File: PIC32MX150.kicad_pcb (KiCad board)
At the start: 2 copper layers, 28 parts, among them J1 GPIO_1, J2 USB_B_Micro, J3 Barrel_Jack, J4 ICSP, J5 GPIO_2, SW1 RST, SW2 SW_SPDT, U1 PIC32MX150F128D-IPT, U2 LM22676MR-ADJ, U3 CH340C

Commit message: LO
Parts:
- added C13: 10p, Capacitor_SMD:C_0603_1608Metric_Pad1.08x0.95mm_HandSolder, F.Cu at (96.3, 54.6)
- added C14: 10p, Capacitor_SMD:C_0603_1608Metric_Pad1.08x0.95mm_HandSolder, F.Cu at (103.5, 61.8)
- added C15: 1u, Capacitor_SMD:C_0603_1608Metric_Pad1.08x0.95mm_HandSolder, F.Cu at (75.8, 52.6)
- added C16: 100n, Capacitor_SMD:C_0603_1608Metric_Pad1.08x0.95mm_HandSolder, F.Cu at (78.6, 52.6)
- added C17: 100n, Capacitor_SMD:C_0603_1608Metric_Pad1.08x0.95mm_HandSolder, F.Cu at (60.6, 47.2)
- added C18: 100n, Capacitor_SMD:C_0603_1608Metric_Pad1.08x0.95mm_HandSolder, F.Cu at (62.1, 88.4)
- added D2: LED_B, LED_SMD:LED_0603_1608Metric_Pad1.05x0.95mm_HandSolder, F.Cu at (56.5, 63.4)
- added D3: LED_B, LED_SMD:LED_0603_1608Metric_Pad1.05x0.95mm_HandSolder, F.Cu at (58.8, 63.4)
- added D4: LED_G, LED_SMD:LED_0603_1608Metric_Pad1.05x0.95mm_HandSolder, F.Cu at (54.5, 53.3)
- added JP1: Jumper_NO_Small, Jumper:SolderJumper-2_P1.3mm_Open_Pad1.0x1.5mm, B.Cu at (108.9, 72.2)
- added R5: 1M, Resistor_SMD:R_0603_1608Metric_Pad0.98x0.95mm_HandSolder, F.Cu at (96.3, 60.8)
- added R6: 1.5K, Resistor_SMD:R_0603_1608Metric_Pad0.98x0.95mm_HandSolder, F.Cu at (60.6, 55.2)
- added R7: 1K, Resistor_SMD:R_0603_1608Metric_Pad0.98x0.95mm_HandSolder, B.Cu at (51.4, 49.3)
- added Y1: TSX3225, Crystal:Crystal_SMD_SeikoEpson_TSX3225-4Pin_3.2x2.5mm_HandSoldering, F.Cu at (100.0, 58.3)
- C12, U3: moved to F.Cu
- C7, R1: moved to B.Cu
- J1: footprint Connector_PinHeader_2.54mm:PinHeader_2x12_P2.54mm_Vertical -> Connector_PinSocket_2.54mm:PinSocket_2x12_P2.54mm_Vertical
- L1: footprint Inductor_SMD:L_0805_2012Metric_Pad1.15x1.40mm_HandSolder -> Inductor_SMD:L_Taiyo-Yuden_MD-1616
- SW2: footprint Button_Switch_THT:SW_Slide_1P2T_CK_OS102011MS2Q -> Custom_Libs:SPDT_SW_Big
- moved D1 51.2 mm to (76.8, 46.2), turned to 0 degrees
- moved L1 50.1 mm to (66.2, 45.2)
- moved R4 48.3 mm to (60.6, 51.1), turned to 270 degrees
- moved C11 48.1 mm to (55.0, 47.1), turned to 90 degrees
- moved C8 42.4 mm to (43.1, 49.4), turned to 90 degrees
- moved C10 41.9 mm to (69.7, 48.3)
- moved C9 38.3 mm to (47.9, 47.1), turned to 90 degrees
- moved R3 37.1 mm to (63.0, 51.1), turned to 90 degrees
- moved U2 35.5 mm to (69.7, 52.3), turned to 0 degrees
- moved U3 20.1 mm to (58.5, 81.3), turned to 270 degrees
- moved J1 14.8 mm to (72.1, 88.9)
- moved J2 12.4 mm to (42.7, 81.5)
- moved SW1 11.9 mm to (106.7, 87.4)
- moved J3 11.8 mm to (50.4, 67.1)
- moved C2 9.85 mm to (98.5, 77.0), turned to 315 degrees
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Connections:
- R1 pad 2: Net-(C7-Pad1) -> Net-(JP1-Pad1)
- R2 pad 2: Net-(C7-Pad1) -> Net-(JP1-Pad1)
- U1 pad 30: (no net) -> /OSC1
- U1 pad 31: (no net) -> /OSC2
- U2 pad 5: (no net) -> GND
- U3 pad 16: +5V -> +3V3
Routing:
- net +3V3: track 0.00 -> 76.6 mm, vias 0 -> 5
- net +5V: track 0.00 -> 49.7 mm
- net /PWR_USB: track 0.00 -> 37.7 mm
- net Net-(J2-Pad2): track 0.00 -> 17.4 mm
- net Net-(J2-Pad3): track 0.00 -> 15.8 mm
- net /OSC1: track 0.00 -> 14.7 mm
- net /PWR_DC: track 0.00 -> 14.0 mm, vias 0 -> 1
- net /OSC2: track 0.00 -> 12.3 mm
- net Net-(D2-Pad1): track 0.00 -> 8.91 mm
- net Net-(R3-Pad1): track 0.00 -> 7.32 mm
- net /MCLR: track 0.00 -> 5.28 mm
- net Net-(D4-Pad1): track 0.00 -> 4.58 mm, vias 0 -> 1
- net Net-(C10-Pad2): track 0.00 -> 3.79 mm
- net Net-(C12-Pad1): track 0.00 -> 2.76 mm
- net GND: vias 0 -> 6
- added copper zone on F.Cu, net +3V3
- added copper zone on F.Cu, net +5V
- added copper zone on F.Cu, net /PWR_DC
- added copper zone on F.Cu, net GND
- added copper zone on F.Cu, net Net-(C10-Pad1)
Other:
- board outline added: 80 x 55 mm
- net class Default: clearance 0.254 -> 0.2032; via_dia 0.508 -> 0.635; via_drill 0.3048 -> 0.381
- net class PWR added: clearance 0.2032, trace_width 0.508, via_dia 0.762, via_drill 0.508
- rule trace_clearance: 0.254 -> 0.2032

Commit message: inductor
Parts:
- removed D2, D3: LED_B, LED_SMD:LED_0603_1608Metric_Pad1.05x0.95mm_HandSolder
- removed R6: 1.5K, Resistor_SMD:R_0603_1608Metric_Pad0.98x0.95mm_HandSolder
- L1: value 8.2u -> 22u; footprint Inductor_SMD:L_Taiyo-Yuden_MD-1616 -> Inductor_SMD:L_Taiyo-Yuden_NR-80xx_HandSoldering
- moved C18 13.0 mm to (61.6, 75.4), turned to 90 degrees
- moved C12 10.1 mm to (49.6, 78.4), turned to 180 degrees
- moved R3 6.59 mm to (59.9, 56.9)
- moved U2 6.56 mm to (66.3, 57.9)
- moved J5 6.48 mm to (111.5, 45.0)
- moved R4 6.32 mm to (58.2, 56.9)
- moved C17 6.28 mm to (59.1, 53.3), turned to 0 degrees
- moved C10 6.13 mm to (66.3, 53.3)
- moved C16 5.58 mm to (73.4, 54.5), turned to 0 degrees
- moved C15 5.32 mm to (73.4, 57.3), turned to 0 degrees
- moved C8 5.12 mm to (46.4, 53.3), turned to 180 degrees
- moved R7 4.13 mm to (48.8, 52.4)
- moved D1 3.91 mm to (75.9, 50.0)
- moved U3 3.71 mm to (55.6, 79.0), turned to 0 degrees
- moved L1 2.45 mm to (65.3, 47.5)
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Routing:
- net +3V3: track 76.6 -> 99.0 mm, vias 5 -> 4
- net /PWR_DC: track 14.0 -> 0.00 mm, vias 1 -> 0
- net /PWR_USB: track 37.7 -> 27.2 mm, vias 0 -> 1
- net Net-(D2-Pad1): track 8.91 -> 0.00 mm
- net Net-(J2-Pad2): track 17.4 -> 9.03 mm
- net Net-(J2-Pad3): track 15.8 -> 18.2 mm
- net /MCLR: track 5.28 -> 3.89 mm
- net /OSC2: track 12.3 -> 11.0 mm
- net GND: track 0.00 -> 1.22 mm, vias 6 -> 42
- net Net-(R3-Pad1): track 7.32 -> 6.18 mm
- net Net-(D4-Pad1): track 4.58 -> 3.44 mm
- net /OSC1: track 14.7 -> 13.7 mm
- net +5V: track 49.7 -> 50.6 mm
- added copper zone on B.Cu, net GND
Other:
- net class Default: via_dia 0.635 -> 0.508; via_drill 0.381 -> 0.3048

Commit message: gerber
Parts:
- added D2: LED_R, LED_SMD:LED_0603_1608Metric_Pad1.05x0.95mm_HandSolder, F.Cu at (108.5, 52.6)
- added D3: LED_B, LED_SMD:LED_0603_1608Metric_Pad1.05x0.95mm_HandSolder, F.Cu at (105.4, 52.6)
- added D5: LED_R, LED_SMD:LED_0603_1608Metric_Pad1.05x0.95mm_HandSolder, F.Cu at (65.7, 80.5)
- added D6: LED_B, LED_SMD:LED_0603_1608Metric_Pad1.05x0.95mm_HandSolder, F.Cu at (63.4, 80.5)
- added G***: LOGO, Custom_Libs:microchip_logo, F.Cu at (63.2, 65.5)
- added G***: LOGO, Custom_Libs:PIC32_Logo, F.Cu at (64.3, 68.3)
- added G***: LOGO, Custom_Libs:OS_Hardware, F.Cu at (106.2, 83.1)
- added J6: SPI_0, Connector_Molex:Molex_PicoBlade_53261-0471_1x04-1MP_P1.25mm_Horizontal, F.Cu at (63.2, 90.7)
- added J7: SPI_1, Connector_Molex:Molex_PicoBlade_53261-0471_1x04-1MP_P1.25mm_Horizontal, F.Cu at (49.0, 90.7)
- added R10: 1K, Resistor_SMD:R_0603_1608Metric_Pad0.98x0.95mm_HandSolder, F.Cu at (61.1, 80.5)
- added R11: 50K, Resistor_SMD:R_0603_1608Metric_Pad0.98x0.95mm_HandSolder, F.Cu at (116.3, 63.0)
- added R6: 1K, Resistor_SMD:R_0603_1608Metric_Pad0.98x0.95mm_HandSolder, B.Cu at (108.6, 56.9)
- added R8: 1K, Resistor_SMD:R_0603_1608Metric_Pad0.98x0.95mm_HandSolder, B.Cu at (108.6, 58.9)
- added R9: 1K, Resistor_SMD:R_0603_1608Metric_Pad0.98x0.95mm_HandSolder, F.Cu at (67.9, 80.5)
- added SW3: SW_SPST, Button_Switch_SMD:SW_SPST_PTS645, F.Cu at (114.8, 52.6)
- L1: footprint Inductor_SMD:L_Taiyo-Yuden_NR-80xx_HandSoldering -> Inductor_SMD:L_Sumida_CDMC6D28_7.25x6.5mm
- SW1: footprint Button_Switch_THT:SW_TH_Tactile_Omron_B3F-10xx -> Button_Switch_SMD:SW_SPST_B3U-1000P
- moved SW1 15.5 mm to (109.7, 72.1)
- moved JP1 5.45 mm to (104.6, 75.7), turned to 90 degrees
- moved C1 4.72 mm to (99.1, 63.8)
- moved R1 4.57 mm to (101.1, 76.7), turned to 0 degrees
- moved C7 4.53 mm to (101.1, 74.7), turned to 180 degrees
- moved C5 3.97 mm to (97.5, 62.2)
- moved U1 3.45 mm to (87.9, 67.2)
- moved R2 3.45 mm to (96.4, 72.8)
- moved R5 3.45 mm to (93.5, 58.8)
- moved C13 3.45 mm to (93.8, 53.2)
- moved C2 3.45 mm to (95.0, 74.3)
- moved C3 3.45 mm to (79.1, 58.3)
- moved C14 3.45 mm to (100.6, 59.2)
- moved C4 3.45 mm to (81.1, 60.3)
- moved Y1 3.45 mm to (97.2, 56.2)
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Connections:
- net /RB2 renamed /RB2|SDA2
- net /RB3 renamed /RB3|SCL2
- J1 pad 10: GND -> /RC8|SDI1
- J1 pad 11: /RA7 -> /RB12
- J1 pad 12: /RB12 -> /RB10
- J1 pad 13: /AN0 -> /RB13|U1RX
- J1 pad 14: /AN1 -> /RB11
- J1 pad 15: /RC9 -> /RA10
- J1 pad 16: /RC7 -> GND
- J1 pad 17: /RC8 -> /RB14|SCK1
- J1 pad 18: (no net) -> /RA7
- J1 pad 19: (no net) -> /AN0
- J1 pad 2: /RC6 -> GND
- J1 pad 20: /RB14 -> /RB15|U1TX
- J1 pad 22: /RB15 -> /AN1
- J1 pad 3: /RB9 -> /RB8|U2RX
- J1 pad 4: /RB10 -> /RB7|SS1
- J1 pad 5: /RB13 -> GND
- J1 pad 6: /RB6 -> /RB9|U2TX
- J1 pad 7: /RB5 -> /RC7
- J1 pad 8: /RB11 -> /RC6|SDO1
- J1 pad 9: /RA10 -> /RC9
- J5 pad 13: /RB7 -> /RB5
- J5 pad 14: /RB8 -> /RB6
- U1 pad 1: /RB9 -> /RB9|U2TX
- U1 pad 11: /RB13 -> /RB13|U1RX
- U1 pad 14: /RB14 -> /RB14|SCK1
- U1 pad 15: /RB15 -> /RB15|U1TX
- U1 pad 2: /RC6 -> /RC6|SDO1
- U1 pad 4: /RC8 -> /RC8|SDI1
- U1 pad 43: /RB7 -> /RB7|SS1
- U1 pad 44: /RB8 -> /RB8|U2RX
- U3 pad 2: (no net) -> /RB13|U1RX
- U3 pad 3: (no net) -> /RB15|U1TX
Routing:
- net +3V3: track 99.0 -> 256.6 mm, vias 4 -> 6
- net +5V: track 50.6 -> 163.1 mm, vias 0 -> 1
- net /RB14|SCK1: track 0.00 -> 77.8 mm, vias 0 -> 3
- net /RB15|U1TX: track 0.00 -> 69.4 mm, vias 0 -> 4
- net /RC8|SDI1: track 0.00 -> 65.7 mm, vias 0 -> 3
- net /RB10: track 0.00 -> 63.8 mm
- net /RB13|U1RX: track 0.00 -> 61.9 mm, vias 0 -> 4
- net /RC6|SDO1: track 0.00 -> 60.6 mm, vias 0 -> 3
- net /RB7|SS1: track 0.00 -> 53.8 mm, vias 0 -> 2
- net /RC0: track 0.00 -> 49.7 mm, vias 0 -> 1
- net /RC1: track 0.00 -> 32.4 mm, vias 0 -> 1
- net /RB8|U2RX: track 0.00 -> 31.2 mm, vias 0 -> 1
- net /RC2: track 0.00 -> 30.8 mm, vias 0 -> 1
- net /RB2|SDA2: track 0.00 -> 27.9 mm, vias 0 -> 1
- net /PGC: track 0.00 -> 26.8 mm, vias 0 -> 1
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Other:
- outline, holes or cut-outs redrawn
- net class Default removed
- net class PWR removed

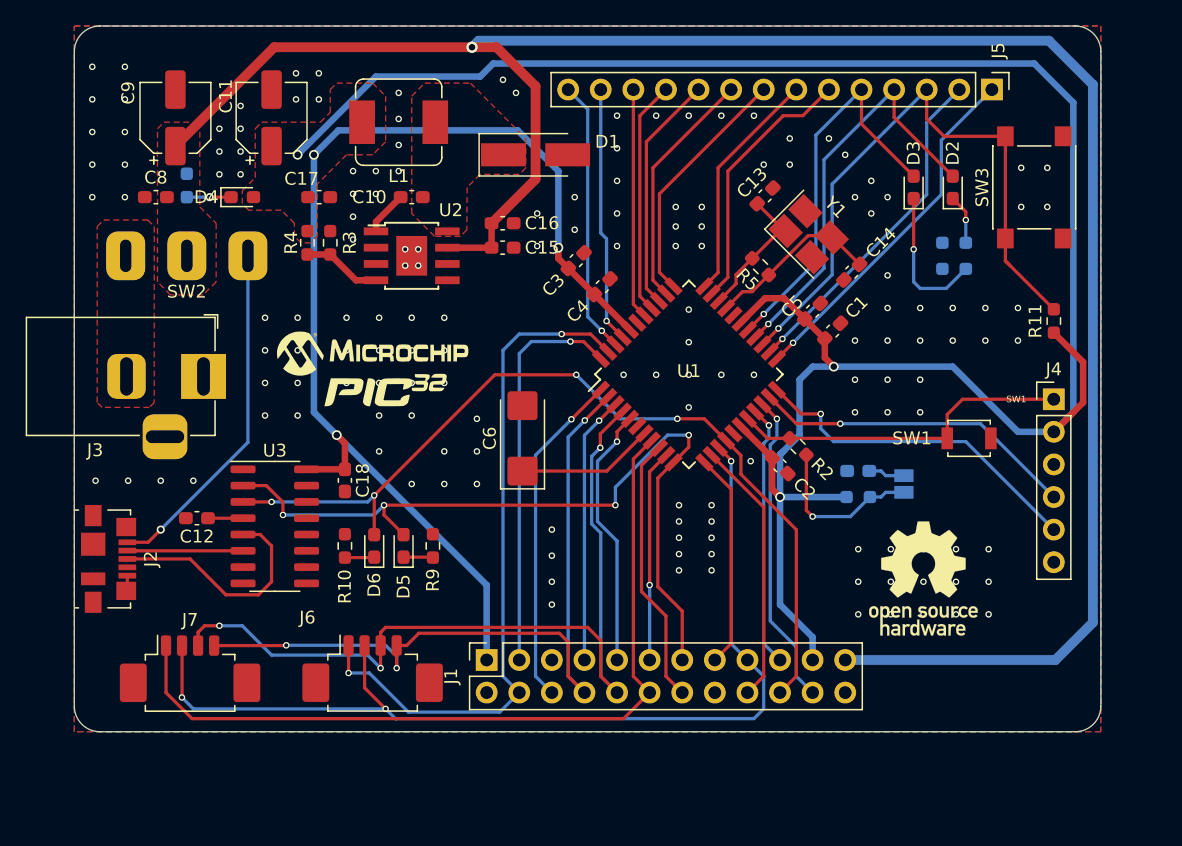
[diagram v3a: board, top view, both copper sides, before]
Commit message: LM22676 active-high
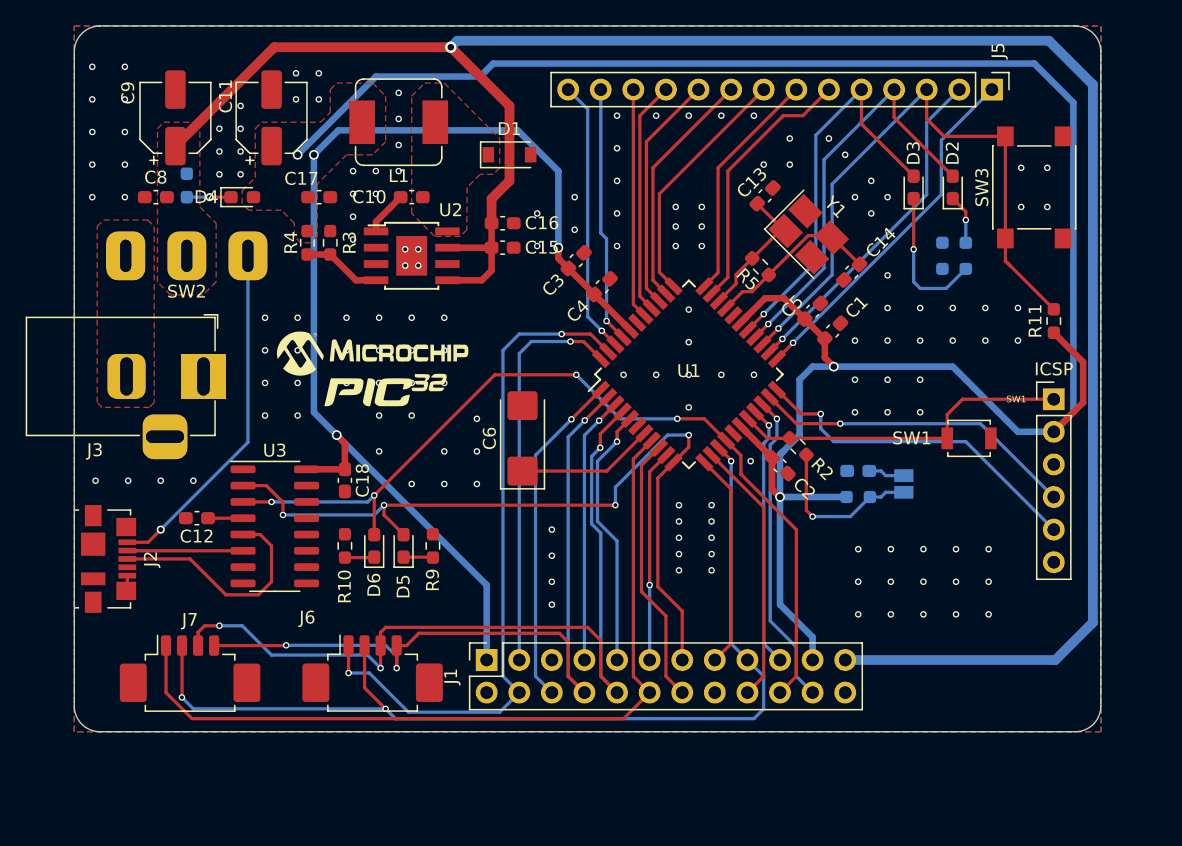
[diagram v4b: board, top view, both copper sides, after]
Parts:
- removed the G*** at (106.2, 83.1)
- D1: footprint Diode_SMD:D_SMA_Handsoldering -> Diode_SMD:D_SOD-123
- moved D1 2.03 mm to (73.9, 50.0)
- renumbered J4 to ICSP
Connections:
- ICSP pad 6: (no net) -> unconnected-(J4-Pad6)
- J2 pad 4: (no net) -> unconnected-(J2-Pad4)
- U2 pad 2: (no net) -> unconnected-(U2-Pad2)
- U2 pad 3: (no net) -> unconnected-(U2-Pad3)
- U2 pad 5: GND -> +5V
- U3 pad 10: (no net) -> unconnected-(U3-Pad10)
- U3 pad 11: (no net) -> unconnected-(U3-Pad11)
- U3 pad 12: (no net) -> unconnected-(U3-Pad12)
- U3 pad 13: (no net) -> unconnected-(U3-Pad13)
- U3 pad 14: (no net) -> unconnected-(U3-Pad14)
- U3 pad 15: (no net) -> unconnected-(U3-Pad15)
- U3 pad 7: (no net) -> unconnected-(U3-Pad7)
- U3 pad 8: (no net) -> unconnected-(U3-Pad8)
- U3 pad 9: (no net) -> unconnected-(U3-Pad9)
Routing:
- net +5V: track 163.1 -> 166.6 mm
- net GND: vias 158 -> 156
